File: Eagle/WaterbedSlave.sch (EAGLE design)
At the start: 4 parts

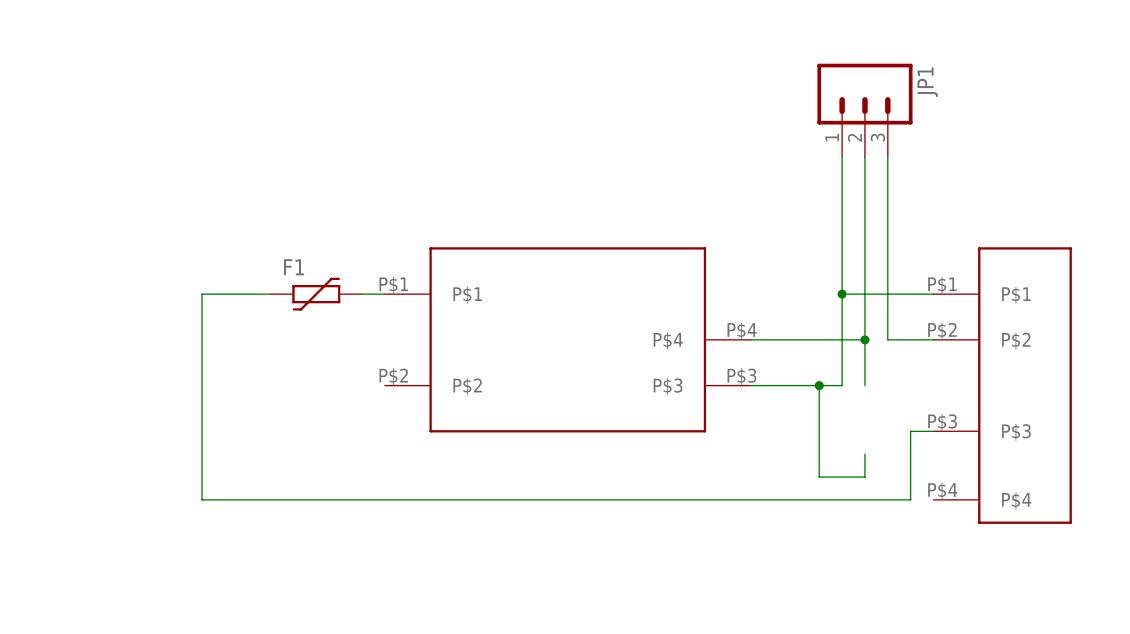
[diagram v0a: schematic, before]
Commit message: Fixed backwards supply footprint
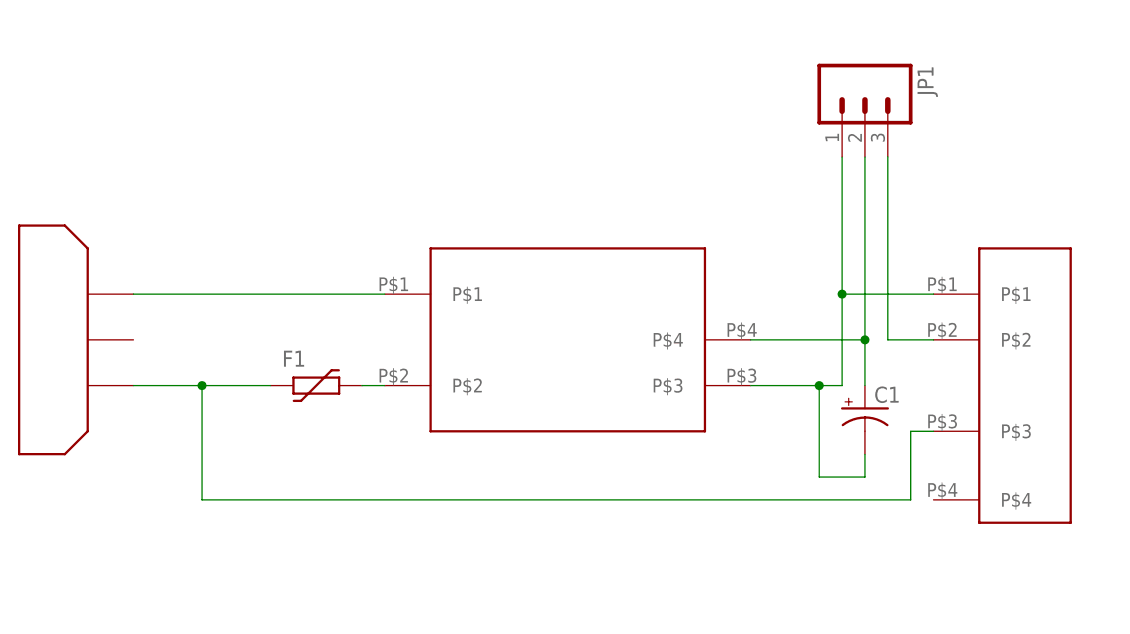
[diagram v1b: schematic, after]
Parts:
- added C1: (no value), resistor:CPOL-USTT5D9
- added U$3: IEC, CuriousTech:IEC
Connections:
- new net N$1: U$1.P$1, U$3.L
- net GND: now also C1.-
- net N$12: now also U$1.P$2; no longer U$1.P$1
- net N$14: now also U$3.H
- net N$15: now also C1.+
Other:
- moved on the sheet: F1
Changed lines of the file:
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@@
 <part name="JP1" library="SparkFun-Connectors" deviceset="M03" device="POLAR_LOCK"/>
 <part name="F1" library="dp_devices" deviceset="FUSE_PTC" device="-1812"/>
+<part name="C1" library="resistor" deviceset="CPOL-US" device="TT5D9"/>
+<part name="U$3" library="CuriousTech" deviceset="IEC" device=""/>
 </parts>
 <sheets>
@@
 <instance part="U$2" gate="G$1" x="111.76" y="55.88" rot="R270"/>
 <instance part="JP1" gate="G$1" x="93.98" y="88.9" rot="R270"/>
-<instance part="F1" gate="G$1" x="33.02" y="66.04"/>
+<instance part="F1" gate="G$1" x="33.02" y="55.88"/>
+<instance part="C1" gate="G$1" x="93.98" y="53.34"/>
+<instance part="U$3" gate="G$1" x="7.62" y="60.96" rot="MR270"/>
 </instances>
 <busses>
@@
 <wire x1="93.98" y1="45.72" x2="93.98" y2="48.26" width="0.1524" layer="91"/>
 <junction x="88.9" y="55.88"/>
+<pinref part="C1" gate="G$1" pin="-"/>
 </segment>
 </net>
@@
 <wire x1="93.98" y1="60.96" x2="93.98" y2="55.88" width="0.1524" layer="91"/>
 <junction x="93.98" y="60.96"/>
+<pinref part="C1" gate="G$1" pin="+"/>
 </segment>
 </net>
@@
 </segment>
 </net>
-<net name="N$12" class="0">
-<segment>
-<pinref part="F1" gate="G$1" pin="2"/>
-<pinref part="U$1" gate="G$1" pin="P$1"/>
-<wire x1="38.1" y1="66.04" x2="40.64" y2="66.04" width="0.1524" layer="91"/>
-</segment>
-</net>
 <net name="N$14" class="0">
 <segment>
 <pinref part="F1" gate="G$1" pin="1"/>
-<wire x1="27.94" y1="66.04" x2="20.32" y2="66.04" width="0.1524" layer="91"/>
-<wire x1="20.32" y1="66.04" x2="20.32" y2="43.18" width="0.1524" layer="91"/>
+<wire x1="27.94" y1="55.88" x2="20.32" y2="55.88" width="0.1524" layer="91"/>
+<wire x1="20.32" y1="55.88" x2="20.32" y2="43.18" width="0.1524" layer="91"/>
 <wire x1="20.32" y1="43.18" x2="99.06" y2="43.18" width="0.1524" layer="91"/>
 <wire x1="99.06" y1="43.18" x2="99.06" y2="50.8" width="0.1524" layer="91"/>
 <pinref part="U$2" gate="G$1" pin="P$3"/>
 <wire x1="99.06" y1="50.8" x2="101.6" y2="50.8" width="0.1524" layer="91"/>
+<pinref part="U$3" gate="G$1" pin="H"/>
+<wire x1="12.7" y1="55.88" x2="20.32" y2="55.88" width="0.1524" layer="91"/>
+<junction x="20.32" y="55.88"/>
 </segment>
 </net>
+<net name="N$12" class="0">
+<segment>
+<pinref part="F1" gate="G$1" pin="2"/>
+<pinref part="U$1" gate="G$1" pin="P$2"/>
+<wire x1="38.1" y1="55.88" x2="40.64" y2="55.88" width="0.1524" layer="91"/>
+</segment>
+</net>
+<net name="N$1" class="0">
+<segment>
+<pinref part="U$3" gate="G$1" pin="L"/>
+<pinref part="U$1" gate="G$1" pin="P$1"/>
+<wire x1="12.7" y1="66.04" x2="40.64" y2="66.04" width="0.1524" layer="91"/>
+</segment>
+</net>

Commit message: Update WaterbedSlave.sch
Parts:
- removed U$1: RAC5A240VAC, CuriousTech:RAC5A240VAC
- added JP2, JP3: (no value), SparkFun-Connectors:M01PTH_2MM
- added SUPP: RAC02-3.3SC, CuriousTech:RAC02-3.3SC
- C1: value (none) -> 330uF
- U$3: value IEC -> IEC 0714-7-E
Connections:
- new net N$6: JP2.1, U$2.AC1
- net GND: now also SUPP.3V3, U$2._DC-; no longer U$1.P$3, U$2.P$1
- net N$1: now also JP3.1, SUPP.AC1; no longer U$1.P$1
- net N$12: now also SUPP.AC2; no longer U$1.P$2
- net N$14: now also U$2.AC2; no longer U$2.P$3
- net N$15: now also SUPP.GND; no longer U$1.P$4
- net N$16: now also U$2._DC+; no longer U$2.P$2
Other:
- moved on the sheet: C1, JP1
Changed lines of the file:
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@@
 </classes>
 <parts>
-<part name="U$1" library="CuriousTech" deviceset="RAC5A240VAC" device=""/>
 <part name="U$2" library="CuriousTech" deviceset="SSR-5A-240VAC" device=""/>
 <part name="JP1" library="SparkFun-Connectors" deviceset="M03" device="POLAR_LOCK"/>
 <part name="F1" library="dp_devices" deviceset="FUSE_PTC" device="-1812"/>
-<part name="C1" library="resistor" deviceset="CPOL-US" device="TT5D9"/>
-<part name="U$3" library="CuriousTech" deviceset="IEC" device=""/>
+<part name="C1" library="resistor" deviceset="CPOL-US" device="TT5D9" value="330uF"/>
+<part name="U$3" library="CuriousTech" deviceset="IEC" device="" value="IEC 0714-7-E"/>
+<part name="SUPP" library="CuriousTech" deviceset="RAC02-3.3SC" device=""/>
+<part name="JP3" library="SparkFun-Connectors" deviceset="M01" device="PTH_2MM"/>
+<part name="JP2" library="SparkFun-Connectors" deviceset="M01" device="PTH_2MM"/>
 </parts>
 <sheets>
@@
 </plain>
 <instances>
-<instance part="U$1" gate="G$1" x="60.96" y="60.96"/>
 <instance part="U$2" gate="G$1" x="111.76" y="55.88" rot="R270"/>
-<instance part="JP1" gate="G$1" x="93.98" y="88.9" rot="R270"/>
+<instance part="JP1" gate="G$1" x="91.44" y="93.98" rot="R270"/>
 <instance part="F1" gate="G$1" x="33.02" y="55.88"/>
-<instance part="C1" gate="G$1" x="93.98" y="53.34"/>
-<instance part="U$3" gate="G$1" x="7.62" y="60.96" rot="MR270"/>
+<instance part="C1" gate="G$1" x="83.82" y="76.2"/>
+<instance part="U$3" gate="G$1" x="17.78" y="55.88" rot="MR180"/>
+<instance part="SUPP" gate="G$1" x="60.96" y="60.96"/>
+<instance part="JP3" gate="G$1" x="60.96" y="33.02" rot="R90"/>
+<instance part="JP2" gate="G$1" x="68.58" y="33.02" rot="R90"/>
 </instances>
 <busses>
@@
 <net name="GND" class="0">
 <segment>
-<pinref part="U$1" gate="G$1" pin="P$3"/>
-<wire x1="81.28" y1="55.88" x2="88.9" y2="55.88" width="0.1524" layer="91"/>
 <pinref part="JP1" gate="G$1" pin="1"/>
-<pinref part="U$2" gate="G$1" pin="P$1"/>
-<wire x1="88.9" y1="55.88" x2="91.44" y2="55.88" width="0.1524" layer="91"/>
-<wire x1="91.44" y1="66.04" x2="91.44" y2="81.28" width="0.1524" layer="91"/>
-<wire x1="101.6" y1="66.04" x2="91.44" y2="66.04" width="0.1524" layer="91"/>
-<wire x1="91.44" y1="66.04" x2="91.44" y2="55.88" width="0.1524" layer="91"/>
-<junction x="91.44" y="66.04"/>
-<wire x1="88.9" y1="55.88" x2="88.9" y2="45.72" width="0.1524" layer="91"/>
-<wire x1="88.9" y1="45.72" x2="93.98" y2="45.72" width="0.1524" layer="91"/>
-<wire x1="93.98" y1="45.72" x2="93.98" y2="48.26" width="0.1524" layer="91"/>
-<junction x="88.9" y="55.88"/>
+<pinref part="U$2" gate="G$1" pin="_DC-"/>
+<wire x1="88.9" y1="66.04" x2="88.9" y2="86.36" width="0.1524" layer="91"/>
+<wire x1="101.6" y1="66.04" x2="88.9" y2="66.04" width="0.1524" layer="91"/>
+<junction x="88.9" y="66.04"/>
 <pinref part="C1" gate="G$1" pin="-"/>
+<wire x1="83.82" y1="66.04" x2="83.82" y2="71.12" width="0.1524" layer="91"/>
+<wire x1="81.28" y1="66.04" x2="83.82" y2="66.04" width="0.1524" layer="91"/>
+<wire x1="83.82" y1="66.04" x2="88.9" y2="66.04" width="0.1524" layer="91"/>
+<junction x="83.82" y="66.04"/>
+<pinref part="SUPP" gate="G$1" pin="3V3"/>
 </segment>
 </net>
 <net name="N$15" class="0">
 <segment>
-<pinref part="U$1" gate="G$1" pin="P$4"/>
-<wire x1="81.28" y1="60.96" x2="93.98" y2="60.96" width="0.1524" layer="91"/>
+<wire x1="81.28" y1="60.96" x2="91.44" y2="60.96" width="0.1524" layer="91"/>
 <pinref part="JP1" gate="G$1" pin="2"/>
-<wire x1="93.98" y1="60.96" x2="93.98" y2="81.28" width="0.1524" layer="91"/>
-<wire x1="93.98" y1="60.96" x2="93.98" y2="55.88" width="0.1524" layer="91"/>
-<junction x="93.98" y="60.96"/>
+<wire x1="91.44" y1="60.96" x2="91.44" y2="81.28" width="0.1524" layer="91"/>
+<pinref part="SUPP" gate="G$1" pin="GND"/>
 <pinref part="C1" gate="G$1" pin="+"/>
+<wire x1="91.44" y1="81.28" x2="91.44" y2="86.36" width="0.1524" layer="91"/>
+<wire x1="83.82" y1="78.74" x2="83.82" y2="81.28" width="0.1524" layer="91"/>
+<wire x1="83.82" y1="81.28" x2="91.44" y2="81.28" width="0.1524" layer="91"/>
+<junction x="91.44" y="81.28"/>
 </segment>
 </net>
@@
 <segment>
 <pinref part="JP1" gate="G$1" pin="3"/>
-<wire x1="96.52" y1="81.28" x2="96.52" y2="60.96" width="0.1524" layer="91"/>
-<pinref part="U$2" gate="G$1" pin="P$2"/>
-<wire x1="96.52" y1="60.96" x2="101.6" y2="60.96" width="0.1524" layer="91"/>
+<wire x1="93.98" y1="86.36" x2="93.98" y2="60.96" width="0.1524" layer="91"/>
+<pinref part="U$2" gate="G$1" pin="_DC+"/>
+<wire x1="93.98" y1="60.96" x2="101.6" y2="60.96" width="0.1524" layer="91"/>
 </segment>
 </net>
@@
 <segment>
 <pinref part="F1" gate="G$1" pin="1"/>
-<wire x1="27.94" y1="55.88" x2="20.32" y2="55.88" width="0.1524" layer="91"/>
-<wire x1="20.32" y1="55.88" x2="20.32" y2="43.18" width="0.1524" layer="91"/>
-<wire x1="20.32" y1="43.18" x2="99.06" y2="43.18" width="0.1524" layer="91"/>
-<wire x1="99.06" y1="43.18" x2="99.06" y2="50.8" width="0.1524" layer="91"/>
-<pinref part="U$2" gate="G$1" pin="P$3"/>
-<wire x1="99.06" y1="50.8" x2="101.6" y2="50.8" width="0.1524" layer="91"/>
+<wire x1="27.94" y1="55.88" x2="25.4" y2="55.88" width="0.1524" layer="91"/>
+<wire x1="25.4" y1="55.88" x2="25.4" y2="48.26" width="0.1524" layer="91"/>
+<wire x1="25.4" y1="48.26" x2="96.52" y2="48.26" width="0.1524" layer="91"/>
+<wire x1="96.52" y1="48.26" x2="96.52" y2="50.8" width="0.1524" layer="91"/>
+<pinref part="U$2" gate="G$1" pin="AC2"/>
+<wire x1="96.52" y1="50.8" x2="101.6" y2="50.8" width="0.1524" layer="91"/>
 <pinref part="U$3" gate="G$1" pin="H"/>
-<wire x1="12.7" y1="55.88" x2="20.32" y2="55.88" width="0.1524" layer="91"/>
-<junction x="20.32" y="55.88"/>
+<wire x1="22.86" y1="55.88" x2="25.4" y2="55.88" width="0.1524" layer="91"/>
+<junction x="25.4" y="55.88"/>
 </segment>
 </net>
@@
 <segment>
 <pinref part="F1" gate="G$1" pin="2"/>
-<pinref part="U$1" gate="G$1" pin="P$2"/>
 <wire x1="38.1" y1="55.88" x2="40.64" y2="55.88" width="0.1524" layer="91"/>
+<pinref part="SUPP" gate="G$1" pin="AC2"/>
 </segment>
 </net>
@@
 <segment>
 <pinref part="U$3" gate="G$1" pin="L"/>
-<pinref part="U$1" gate="G$1" pin="P$1"/>
-<wire x1="12.7" y1="66.04" x2="40.64" y2="66.04" width="0.1524" layer="91"/>
+<wire x1="22.86" y1="66.04" x2="35.56" y2="66.04" width="0.1524" layer="91"/>
+<pinref part="SUPP" gate="G$1" pin="AC1"/>
+<wire x1="35.56" y1="66.04" x2="40.64" y2="66.04" width="0.1524" layer="91"/>
+<wire x1="60.96" y1="40.64" x2="60.96" y2="43.18" width="0.1524" layer="91"/>
+<wire x1="60.96" y1="43.18" x2="0" y2="43.18" width="0.1524" layer="91"/>
+<wire x1="0" y1="43.18" x2="0" y2="81.28" width="0.1524" layer="91"/>
+<wire x1="0" y1="81.28" x2="35.56" y2="81.28" width="0.1524" layer="91"/>
+<wire x1="35.56" y1="81.28" x2="35.56" y2="66.04" width="0.1524" layer="91"/>
+<junction x="35.56" y="66.04"/>
+<pinref part="JP3" gate="G$1" pin="1"/>
 </segment>
 </net>
+<net name="N$6" class="0">
+<segment>
+<pinref part="U$2" gate="G$1" pin="AC1"/>
+<wire x1="101.6" y1="43.18" x2="68.58" y2="43.18" width="0.1524" layer="91"/>
+<wire x1="68.58" y1="43.18" x2="68.58" y2="40.64" width="0.1524" layer="91"/>
+<pinref part="JP2" gate="G$1" pin="1"/>
+</segment>
+</net>

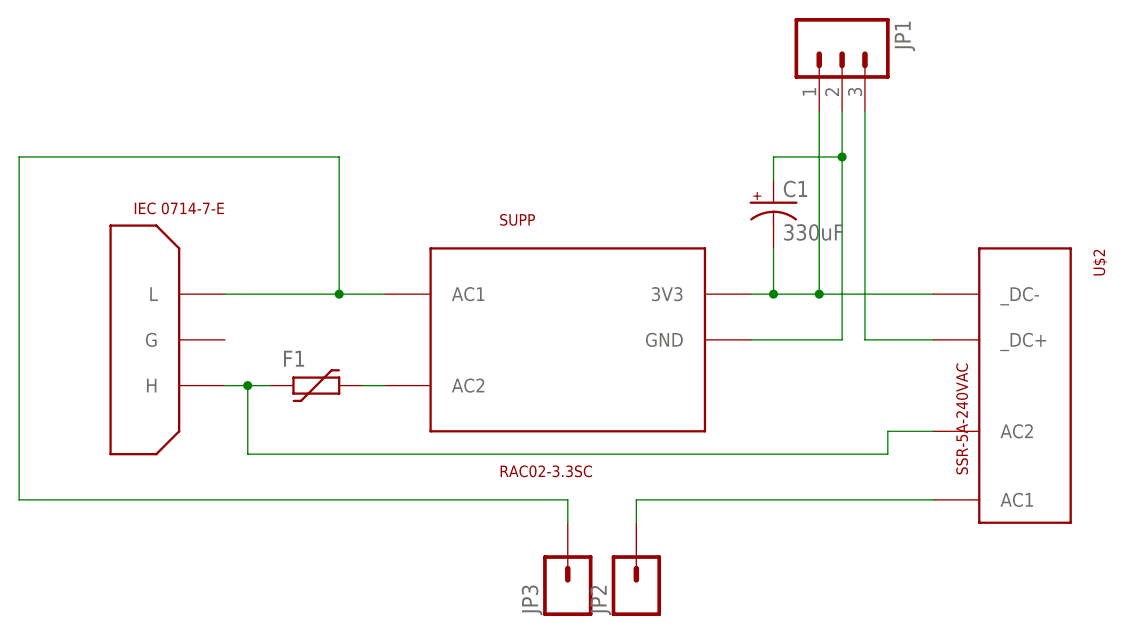
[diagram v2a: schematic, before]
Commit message: Changed PPTC
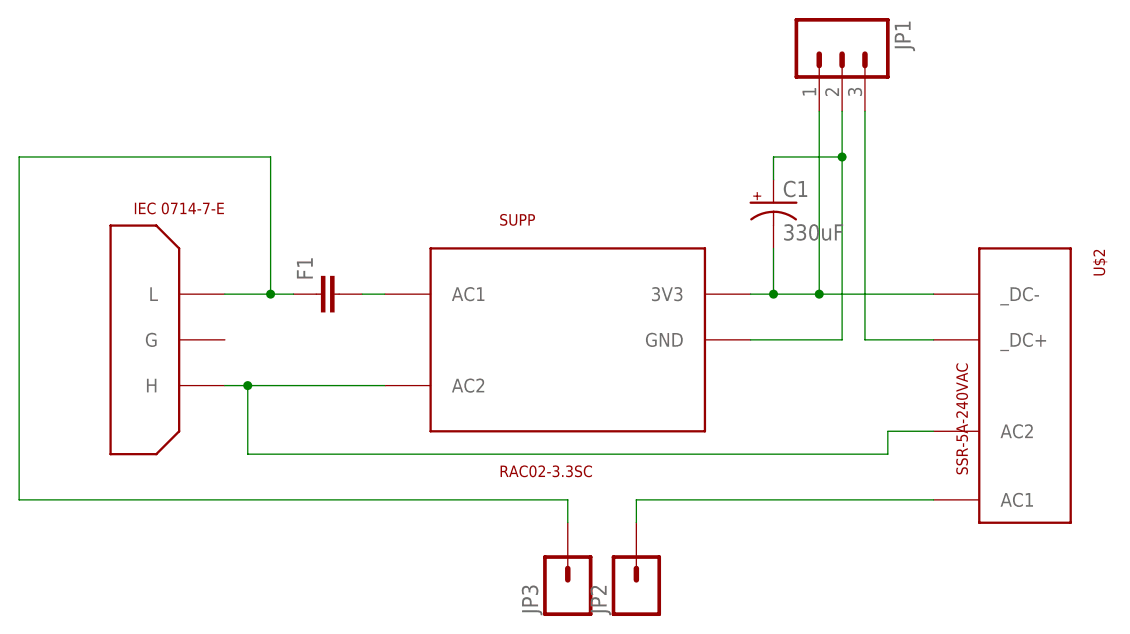
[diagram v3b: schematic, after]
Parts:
- F1: device dp_devices:FUSE_PTC-1812 -> SparkFun-Capacitors:CAPPTH1
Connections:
- removed net N$12: F1.2, SUPP.AC2
- new net N$5: F1.2, SUPP.AC1
- net N$1: now also F1.1; no longer SUPP.AC1
- net N$14: now also SUPP.AC2; no longer F1.1
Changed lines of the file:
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@@
 <?xml version="1.0" encoding="utf-8"?>
 <!DOCTYPE eagle SYSTEM "eagle.dtd">
-<eagle version="7.4.0">
+<eagle version="7.5.0">
 <drawing>
 <settings>
@@
 <part name="U$2" library="CuriousTech" deviceset="SSR-5A-240VAC" device=""/>
 <part name="JP1" library="SparkFun-Connectors" deviceset="M03" device="POLAR_LOCK"/>
-<part name="F1" library="dp_devices" deviceset="FUSE_PTC" device="-1812"/>
 <part name="C1" library="resistor" deviceset="CPOL-US" device="TT5D9" value="330uF"/>
 <part name="U$3" library="CuriousTech" deviceset="IEC" device="" value="IEC 0714-7-E"/>
@@
 <part name="JP3" library="SparkFun-Connectors" deviceset="M01" device="PTH_2MM"/>
 <part name="JP2" library="SparkFun-Connectors" deviceset="M01" device="PTH_2MM"/>
+<part name="F1" library="SparkFun-Capacitors" deviceset="CAP" device="PTH1"/>
 </parts>
 <sheets>
@@
 <instance part="U$2" gate="G$1" x="111.76" y="55.88" rot="R270"/>
 <instance part="JP1" gate="G$1" x="91.44" y="93.98" rot="R270"/>
-<instance part="F1" gate="G$1" x="33.02" y="55.88"/>
 <instance part="C1" gate="G$1" x="83.82" y="76.2"/>
 <instance part="U$3" gate="G$1" x="17.78" y="55.88" rot="MR180"/>
@@
 <instance part="JP3" gate="G$1" x="60.96" y="33.02" rot="R90"/>
 <instance part="JP2" gate="G$1" x="68.58" y="33.02" rot="R90"/>
+<instance part="F1" gate="G$1" x="35.56" y="66.04" rot="R90"/>
 </instances>
 <busses>
@@
 <net name="N$14" class="0">
 <segment>
-<pinref part="F1" gate="G$1" pin="1"/>
-<wire x1="27.94" y1="55.88" x2="25.4" y2="55.88" width="0.1524" layer="91"/>
 <wire x1="25.4" y1="55.88" x2="25.4" y2="48.26" width="0.1524" layer="91"/>
 <wire x1="25.4" y1="48.26" x2="96.52" y2="48.26" width="0.1524" layer="91"/>
@@
 <pinref part="U$3" gate="G$1" pin="H"/>
 <wire x1="22.86" y1="55.88" x2="25.4" y2="55.88" width="0.1524" layer="91"/>
+<pinref part="SUPP" gate="G$1" pin="AC2"/>
+<wire x1="25.4" y1="55.88" x2="40.64" y2="55.88" width="0.1524" layer="91"/>
 <junction x="25.4" y="55.88"/>
 </segment>
 </net>
-<net name="N$12" class="0">
-<segment>
-<pinref part="F1" gate="G$1" pin="2"/>
-<wire x1="38.1" y1="55.88" x2="40.64" y2="55.88" width="0.1524" layer="91"/>
-<pinref part="SUPP" gate="G$1" pin="AC2"/>
-</segment>
-</net>
 <net name="N$1" class="0">
 <segment>
 <pinref part="U$3" gate="G$1" pin="L"/>
-<wire x1="22.86" y1="66.04" x2="35.56" y2="66.04" width="0.1524" layer="91"/>
-<pinref part="SUPP" gate="G$1" pin="AC1"/>
-<wire x1="35.56" y1="66.04" x2="40.64" y2="66.04" width="0.1524" layer="91"/>
+<wire x1="22.86" y1="66.04" x2="27.94" y2="66.04" width="0.1524" layer="91"/>
 <wire x1="60.96" y1="40.64" x2="60.96" y2="43.18" width="0.1524" layer="91"/>
 <wire x1="60.96" y1="43.18" x2="0" y2="43.18" width="0.1524" layer="91"/>
 <wire x1="0" y1="43.18" x2="0" y2="81.28" width="0.1524" layer="91"/>
-<wire x1="0" y1="81.28" x2="35.56" y2="81.28" width="0.1524" layer="91"/>
-<wire x1="35.56" y1="81.28" x2="35.56" y2="66.04" width="0.1524" layer="91"/>
-<junction x="35.56" y="66.04"/>
+<wire x1="0" y1="81.28" x2="27.94" y2="81.28" width="0.1524" layer="91"/>
+<wire x1="27.94" y1="81.28" x2="27.94" y2="66.04" width="0.1524" layer="91"/>
 <pinref part="JP3" gate="G$1" pin="1"/>
+<pinref part="F1" gate="G$1" pin="1"/>
+<wire x1="30.48" y1="66.04" x2="27.94" y2="66.04" width="0.1524" layer="91"/>
+<junction x="27.94" y="66.04"/>
 </segment>
 </net>
@@
 </segment>
 </net>
+<net name="N$5" class="0">
+<segment>
+<pinref part="F1" gate="G$1" pin="2"/>
+<pinref part="SUPP" gate="G$1" pin="AC1"/>
+<wire x1="38.1" y1="66.04" x2="40.64" y2="66.04" width="0.1524" layer="91"/>
+</segment>
+</net>
